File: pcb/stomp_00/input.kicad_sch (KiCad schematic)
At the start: 28 parts, among them J2 GuitarInput1, J7 GuitarInput2, U2 TL072

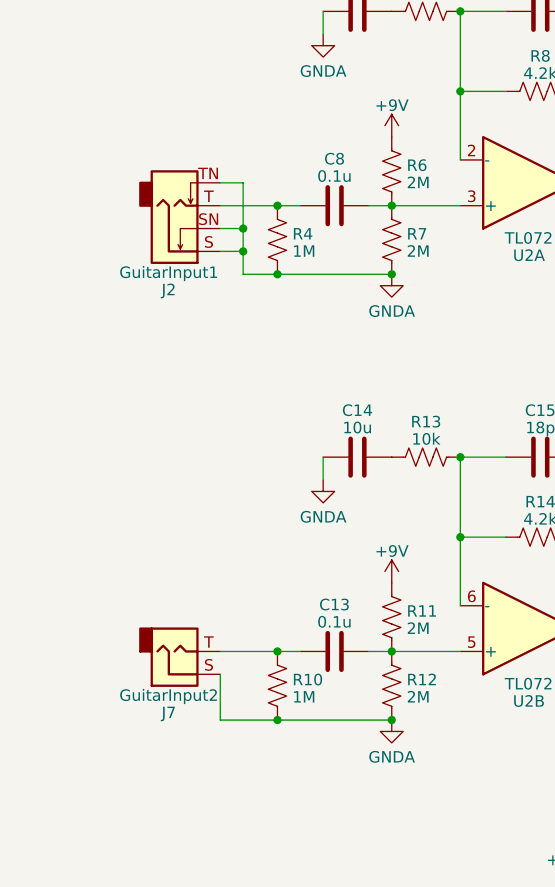
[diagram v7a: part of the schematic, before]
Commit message: footswitch routing
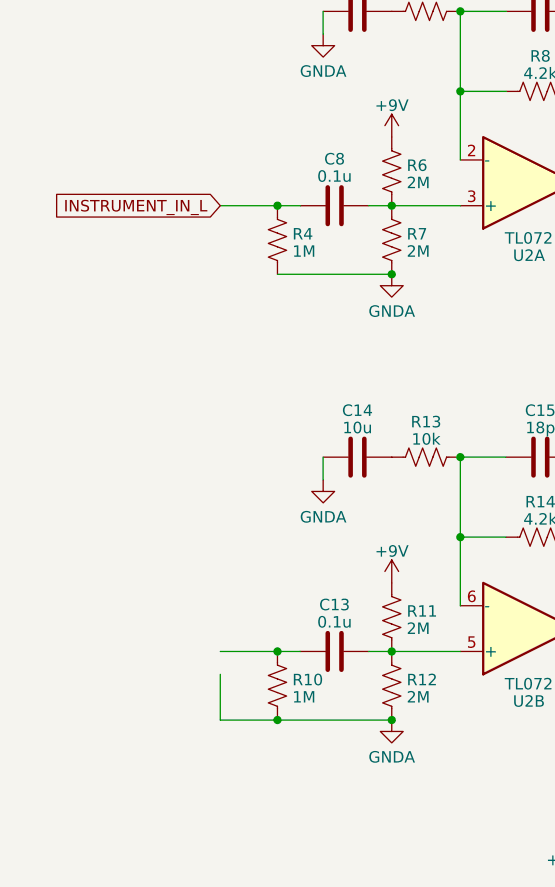
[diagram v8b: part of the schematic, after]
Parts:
- removed J2: GuitarInput1, Connector_Audio:Jack_6.35mm_Neutrik_NMJ4HCD2_Horizontal, symbol Connector_Audio:NMJ4HCD2
- removed J7: GuitarInput2, Connector_PinHeader_2.54mm:PinHeader_1x02_P2.54mm_Vertical, symbol Connector_Audio:AudioJack2
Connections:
- net INSTRUMENT_IN_L: now reaches C8.1, R4.1
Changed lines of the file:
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@@
   (junction (at 137.16 69.85) (diameter 0) (color 0 0 0 0)
   )
-  (junction (at 97.79 85.09) (diameter 0) (color 0 0 0 0)
-  )
   (junction (at 162.56 80.01) (diameter 0) (color 0 0 0 0)
   )
@@
   (junction (at 114.3 132.08) (diameter 0) (color 0 0 0 0)
   )
-  (junction (at 101.6 90.17) (diameter 0) (color 0 0 0 0)
-  )
   (junction (at 137.16 119.38) (diameter 0) (color 0 0 0 0)
   )
@@
   (junction (at 101.6 132.08) (diameter 0) (color 0 0 0 0)
   )
-  (junction (at 97.79 87.63) (diameter 0) (color 0 0 0 0)
-  )
   (junction (at 137.16 80.01) (diameter 0) (color 0 0 0 0)
   )
@@
     (stroke (width 0) (type default))
   )
-  (wire (pts (xy 97.79 90.17) (xy 101.6 90.17))
-    (stroke (width 0) (type default))
-  )
-  (wire (pts (xy 97.79 87.63) (xy 97.79 90.17))
-    (stroke (width 0) (type default))
-  )
   (wire (pts (xy 101.6 90.17) (xy 114.3 90.17))
     (stroke (width 0) (type default))
@@
     (stroke (width 0) (type default))
   )
-  (wire (pts (xy 95.25 85.09) (xy 97.79 85.09))
-    (stroke (width 0) (type default))
-  )
   (wire (pts (xy 114.3 132.08) (xy 121.92 132.08))
     (stroke (width 0) (type default))
@@
     (stroke (width 0) (type default))
   )
-  (wire (pts (xy 97.79 85.09) (xy 97.79 87.63))
-    (stroke (width 0) (type default))
-  )
   (wire (pts (xy 95.25 82.55) (xy 101.6 82.55))
     (stroke (width 0) (type default))
@@
     (stroke (width 0) (type default))
   )
-  (wire (pts (xy 97.79 80.01) (xy 97.79 85.09))
-    (stroke (width 0) (type default))
-  )
   (wire (pts (xy 162.56 129.54) (xy 162.56 115.57))
     (stroke (width 0) (type default))
   )
   (wire (pts (xy 111.76 132.08) (xy 114.3 132.08))
-    (stroke (width 0) (type default))
-  )
-  (wire (pts (xy 95.25 80.01) (xy 97.79 80.01))
-    (stroke (width 0) (type default))
-  )
-  (wire (pts (xy 95.25 87.63) (xy 97.79 87.63))
     (stroke (width 0) (type default))
   )
@@
     (property "Intersheetrefs" "${INTERSHEET_REFS}" (at 177.0168 80.01 0)
       (effects (font (size 1.27 1.27)) (justify left) hide)
+    )
+  )
+  (global_label "INSTRUMENT_IN_L" (shape input) (at 95.25 82.55 180) (fields_autoplaced)
+    (effects (font (size 1.27 1.27)) (justify right))
+    (property "Intersheetrefs" "${INTERSHEET_REFS}" (at 75.8342 82.55 0)
+      (effects (font (size 1.27 1.27)) (justify right) hide)
     )
   )
@@
     )
   )
-  (symbol (lib_id "Connector_Audio:NMJ4HCD2") (at 90.17 82.55 0) (mirror x) (unit 1)
-    (in_bom yes) (on_board yes) (dnp no)
-    (property "Reference" "J2" (at 89.535 91.9099 0)
-      (effects (font (size 1.27 1.27)))
-    )
-    (property "Value" "GuitarInput1" (at 89.535 89.9889 0)
-      (effects (font (size 1.27 1.27)))
-    )
-    (property "Footprint" "Connector_Audio:Jack_6.35mm_Neutrik_NMJ4HCD2_Horizontal" (at 90.17 87.63 0)
-      (effects (font (size 1.27 1.27)) hide)
-    )
-    (property "Datasheet" "https://www.neutrik.com/en/product/nmj4hcd2" (at 90.17 87.63 0)
-      (effects (font (size 1.27 1.27)) hide)
-    )
-    (pin "S")
-    (pin "SN")
-    (pin "T")
-    (pin "TN")
-    (instances
-      (project "stomp_00"
-        (path "/8f4a2eb0-078b-46cb-b534-a4acd11d130e/9942492d-ba8b-45b2-b427-7fe14bedb7e0"
-          (reference "J2") (unit 1)
-        )
-      )
-    )
-  )
   (symbol (lib_id "Device:R_US") (at 118.11 110.49 90) (unit 1)
     (in_bom yes) (on_board yes) (dnp no) (fields_autoplaced)
@@
         )
       )
-    )
-  )
-  (symbol (lib_id "Connector_Audio:AudioJack2") (at 90.17 132.08 0) (mirror x) (unit 1)
-    (in_bom yes) (on_board yes) (dnp no)
-    (property "Reference" "J7" (at 89.535 138.8999 0)
-      (effects (font (size 1.27 1.27)))
-    )
-    (property "Value" "GuitarInput2" (at 89.535 136.9789 0)
-      (effects (font (size 1.27 1.27)))
-    )
-    (property "Footprint" "Connector_PinHeader_2.54mm:PinHeader_1x02_P2.54mm_Vertical" (at 90.17 132.08 0)
-      (effects (font (size 1.27 1.27)) hide)
-    )
-    (property "Datasheet" "~" (at 90.17 132.08 0)
-      (effects (font (size 1.27 1.27)) hide)
-    )
-    (pin "S")
-    (pin "T")
-    (instances
-      (project "stomp_00"
-        (path "/8f4a2eb0-078b-46cb-b534-a4acd11d130e/9942492d-ba8b-45b2-b427-7fe14bedb7e0"
-          (reference "J7") (unit 1)
-        )
-      )
